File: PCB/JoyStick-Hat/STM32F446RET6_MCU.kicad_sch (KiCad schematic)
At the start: 42 parts, among them SW1 TL3301NF260QG, T1 BU2032SM-JJ-GTR, T2 20021121-00010C4LF, T3 0675031020, U1 STM32F446RET6, U11 AT24C16D-STUM-T, X1 ABM3B-8.000MHZ-B2-T, X2 ABS07-32.768KHZ-9-T

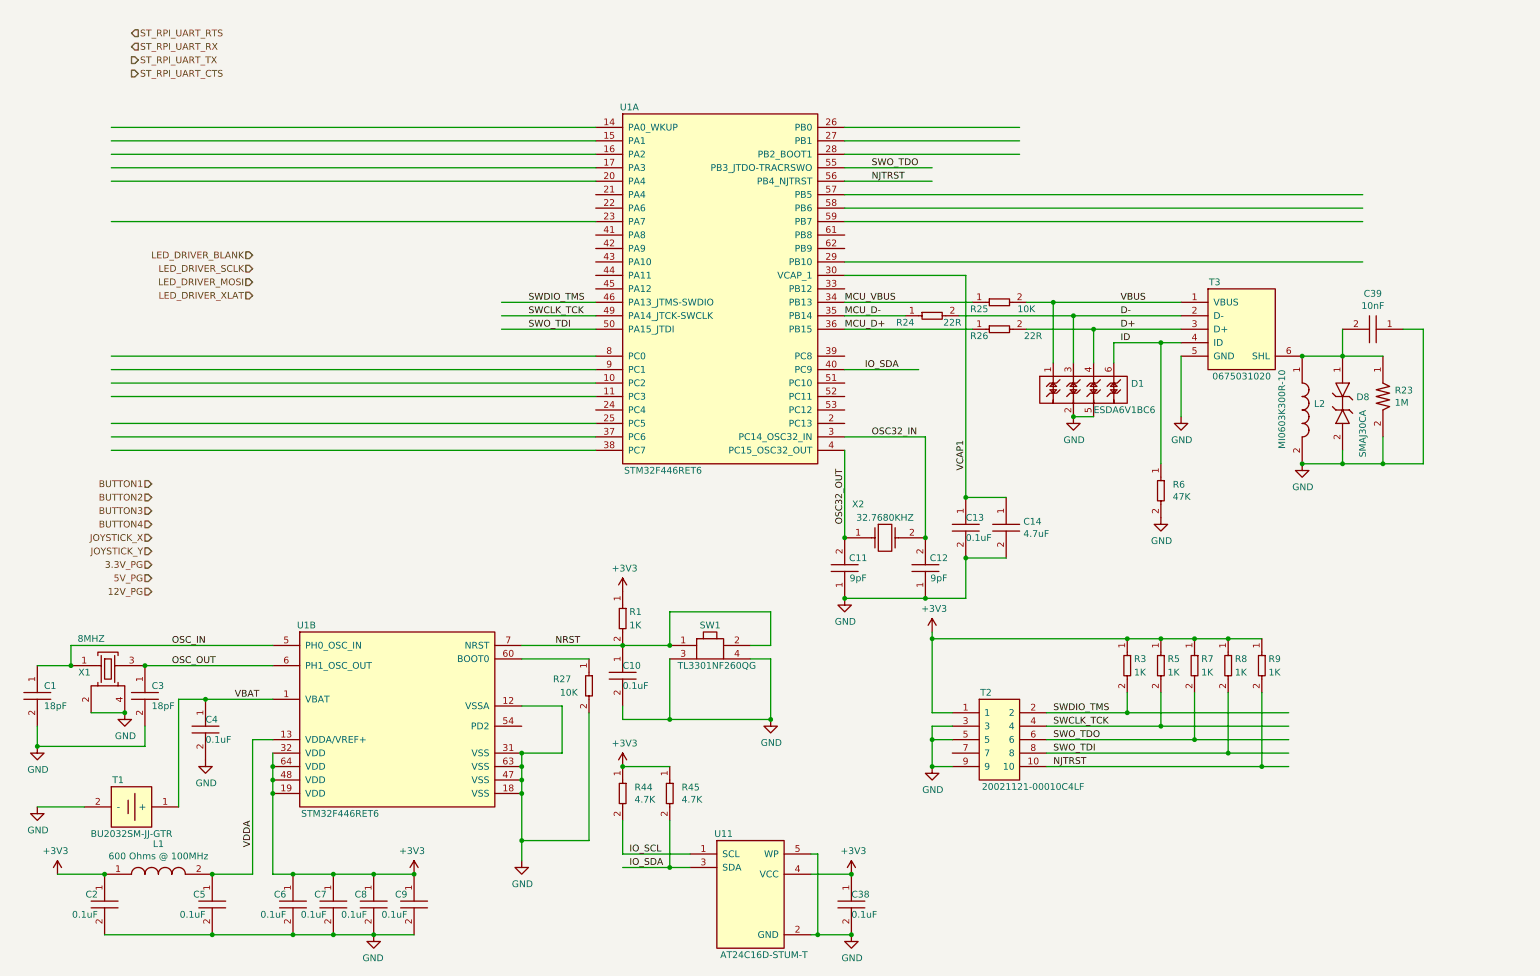
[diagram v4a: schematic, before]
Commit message: Schematic Progress
Made progress with schematic and corrected designator letters with connectors to match the built in paradigm of using J instead of T. T will not be used to referencing transformers instead of connectors.
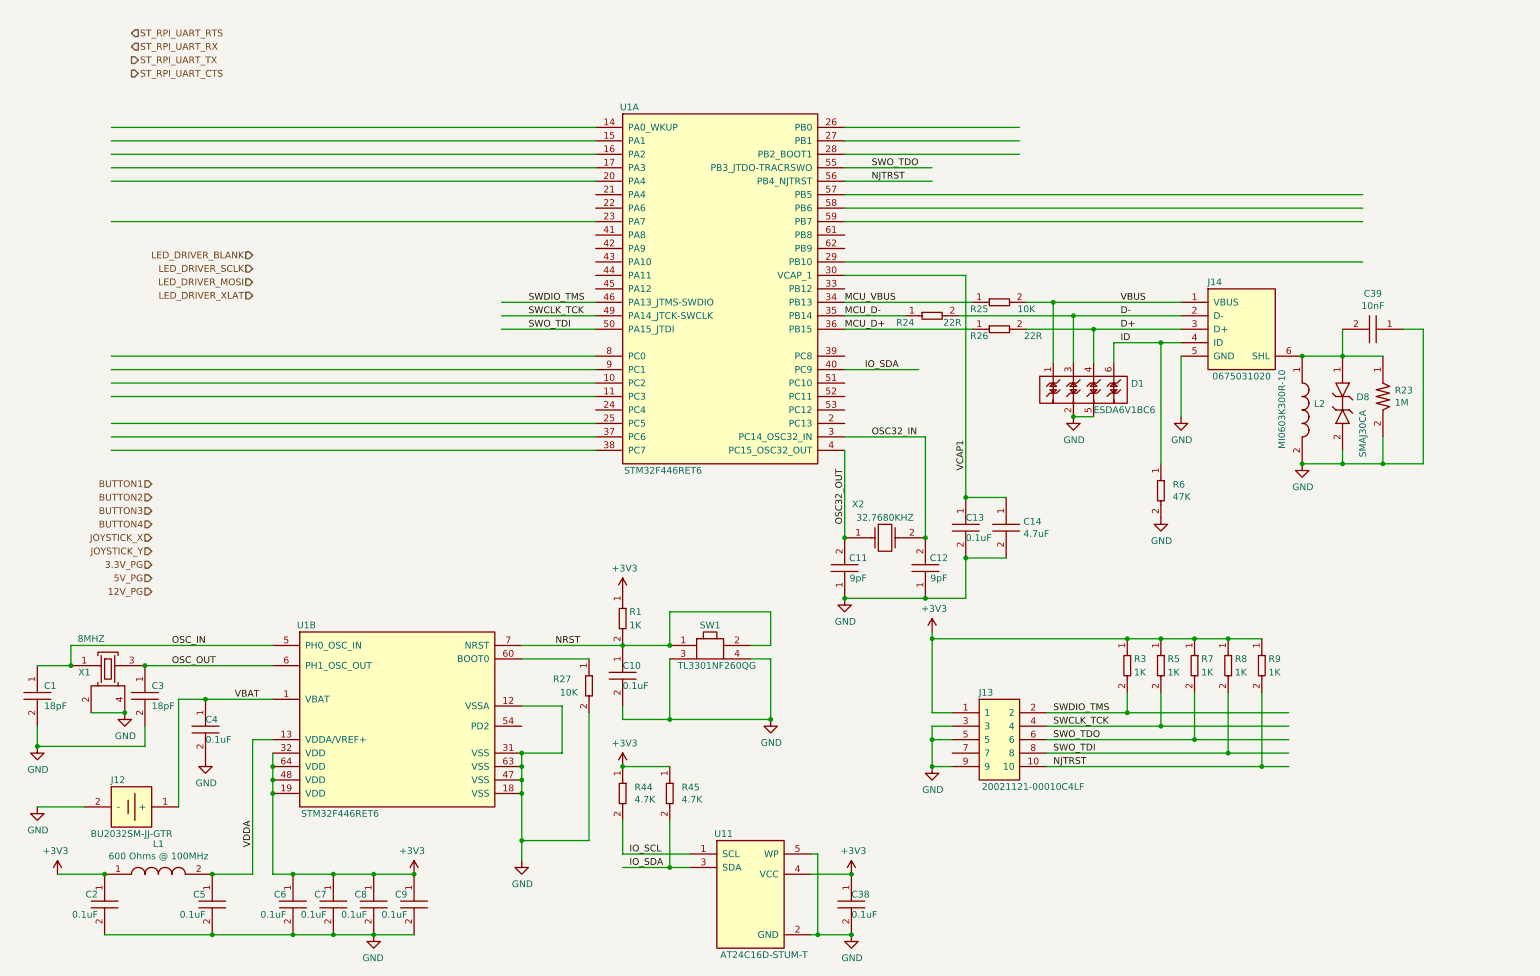
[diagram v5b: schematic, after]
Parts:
- removed T1: BU2032SM-JJ-GTR, AVR-KiCAD-Lib-Battery-Holders:BU2032SM-JJ-GTR, symbol AVR-KiCAD-Lib-Battery-Holders:BU2032SM-JJ-GTR
- added J12: BU2032SM-JJ-GTR, AVR-KiCAD-Lib-Connectors:BU2032SM-JJ-GTR, symbol AVR-KiCAD-Lib-Battery-Holders:BU2032SM-JJ-GTR
- renumbered T2 to J13, T3 to J14
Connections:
- net GND: now also J12.2 (-)
- net VBAT: now also J12.1 (+)
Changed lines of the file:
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@@
     )
   )
-  (symbol (lib_id "AVR-KiCAD-Lib-Battery-Holders:BU2032SM-JJ-GTR") (at 34.29 167.64 0) (unit 1)
-    (in_bom yes) (on_board yes) (dnp no)
-    (property "Reference" "T1" (at 31.75 162.56 0)
-      (effects (font (size 1.27 1.27)))
-    )
-    (property "Value" "BU2032SM-JJ-GTR" (at 34.29 172.72 0)
-      (effects (font (size 1.27 1.27)))
-    )
-    (property "Footprint" "AVR-KiCAD-Lib-Battery-Holders:BU2032SM-JJ-GTR" (at 31.75 158.75 0)
-      (effects (font (size 1.27 1.27)) hide)
-    )
-    (property "Datasheet" "http://www.memoryprotectiondevices.com/datasheets/BU2032SM-JJ-GTR-datasheet.pdf" (at 31.75 165.1 0)
-      (effects (font (size 1.27 1.27)) hide)
-    )
-    (property "Cost QTY: 1" "0.96000" (at 36.83 161.29 0)
-      (effects (font (size 1.27 1.27)) hide)
-    )
-    (property "Cost QTY: 1000" "*" (at 39.37 158.75 0)
-      (effects (font (size 1.27 1.27)) hide)
-    )
-    (property "Cost QTY: 2500" "*" (at 41.91 156.21 0)
-      (effects (font (size 1.27 1.27)) hide)
-    )
-    (property "Cost QTY: 5000" "*" (at 44.45 153.67 0)
-      (effects (font (size 1.27 1.27)) hide)
-    )
-    (property "Cost QTY: 10000" "*" (at 46.99 151.13 0)
-      (effects (font (size 1.27 1.27)) hide)
-    )
-    (property "MFR" "MPD (Memory Protection Devices)" (at 49.53 148.59 0)
-      (effects (font (size 1.27 1.27)) hide)
-    )
-    (property "MFR#" "BU2032SM-JJ-GTR" (at 52.07 146.05 0)
-      (effects (font (size 1.27 1.27)) hide)
-    )
-    (property "Vendor" "Digikey" (at 54.61 143.51 0)
-      (effects (font (size 1.27 1.27)) hide)
-    )
-    (property "Vendor #" "BU2032SM-JJ-GCT-ND" (at 57.15 140.97 0)
-      (effects (font (size 1.27 1.27)) hide)
-    )
-    (property "Designer" "AVR" (at 59.69 138.43 0)
-      (effects (font (size 1.27 1.27)) hide)
-    )
-    (property "Height" "5.3mm" (at 62.23 135.89 0)
-      (effects (font (size 1.27 1.27)) hide)
-    )
-    (property "Date Created" "12/7/2019" (at 90.17 107.95 0)
-      (effects (font (size 1.27 1.27)) hide)
-    )
-    (property "Date Modified" "12/7/2019" (at 64.77 133.35 0)
-      (effects (font (size 1.27 1.27)) hide)
-    )
-    (property "Lead-Free ?" "Yes" (at 67.31 130.81 0)
-      (effects (font (size 1.27 1.27)) hide)
-    )
-    (property "RoHS Levels" "1" (at 69.85 128.27 0)
-      (effects (font (size 1.27 1.27)) hide)
-    )
-    (property "Mounting" "SMT" (at 72.39 125.73 0)
-      (effects (font (size 1.27 1.27)) hide)
-    )
-    (property "Pin Count #" "2" (at 74.93 123.19 0)
-      (effects (font (size 1.27 1.27)) hide)
-    )
-    (property "Status" "Active" (at 77.47 120.65 0)
-      (effects (font (size 1.27 1.27)) hide)
-    )
-    (property "Tolerance" "*" (at 80.01 118.11 0)
-      (effects (font (size 1.27 1.27)) hide)
-    )
-    (property "Type" "Battery Clip" (at 82.55 115.57 0)
-      (effects (font (size 1.27 1.27)) hide)
-    )
-    (property "Voltage" "3.3V" (at 85.09 113.03 0)
-      (effects (font (size 1.27 1.27)) hide)
-    )
-    (property "Package" "Proprietary" (at 87.63 109.22 0)
-      (effects (font (size 1.27 1.27)) hide)
-    )
-    (property "Description" "Battery Holder (Open) Coin, 20.0mm 1 Cell SMD (SMT) Tab" (at 97.79 99.06 0)
-      (effects (font (size 1.27 1.27)) hide)
-    )
-    (property "_Value_" "Battery Clip" (at 92.71 104.14 0)
-      (effects (font (size 1.27 1.27)) hide)
-    )
-    (property "Management_ID" "*" (at 95.25 101.6 0)
-      (effects (font (size 1.27 1.27)) hide)
-    )
-    (pin "1")
-    (pin "2")
-    (instances
-      (project "JoyStick-Hat"
-        (path "/cf0c81b5-5bdf-47c3-83c0-f6980f515e65/edccb318-6986-4250-98d3-482c4b5ba7f8"
-          (reference "T1") (unit 1)
-        )
-      )
-      (project "agricoltura-vine"
-        (path "/d9101753-24ed-41f7-9f75-798d6e08c38a/00000000-0000-0000-0000-00005ee8264d"
-          (reference "T1") (unit 1)
-        )
-      )
-    )
-  )
   (symbol (lib_id "AVR-KiCAD-Lib-Oscillators-Clocks:ABM3B-8.000MHZ-B2-T") (at 27.94 138.43 0) (unit 1)
     (in_bom yes) (on_board yes) (dnp no)
@@
   (symbol (lib_id "AVR-KiCAD-Lib-Connectors:20021121-00010C4LF") (at 194.31 147.32 0) (unit 1)
     (in_bom yes) (on_board yes) (dnp no)
-    (property "Reference" "T2" (at 195.58 146.05 0)
+    (property "Reference" "J13" (at 195.58 146.05 0)
       (effects (font (size 1.27 1.27)))
     )
@@
       (project "JoyStick-Hat"
         (path "/cf0c81b5-5bdf-47c3-83c0-f6980f515e65/edccb318-6986-4250-98d3-482c4b5ba7f8"
-          (reference "T2") (unit 1)
+          (reference "J13") (unit 1)
         )
       )
@@
   (symbol (lib_id "AVR-KiCAD-Lib-Connectors:0675031020") (at 237.49 69.85 0) (unit 1)
     (in_bom yes) (on_board yes) (dnp no)
-    (property "Reference" "T3" (at 238.76 68.58 0)
+    (property "Reference" "J14" (at 238.76 68.58 0)
       (effects (font (size 1.27 1.27)))
     )
@@
       (project "JoyStick-Hat"
         (path "/cf0c81b5-5bdf-47c3-83c0-f6980f515e65/edccb318-6986-4250-98d3-482c4b5ba7f8"
-          (reference "T3") (unit 1)
+          (reference "J14") (unit 1)
         )
       )
@@
         )
       )
+    )
+  )
+  (symbol (lib_id "AVR-KiCAD-Lib-Battery-Holders:BU2032SM-JJ-GTR") (at 34.29 167.64 0) (unit 1)
+    (in_bom yes) (on_board yes) (dnp no)
+    (property "Reference" "J12" (at 31.75 162.56 0)
+      (effects (font (size 1.27 1.27)))
+    )
+    (property "Value" "BU2032SM-JJ-GTR" (at 34.29 172.72 0)
+      (effects (font (size 1.27 1.27)))
+    )
+    (property "Footprint" "AVR-KiCAD-Lib-Connectors:BU2032SM-JJ-GTR" (at 31.75 158.75 0)
+      (effects (font (size 1.27 1.27)) hide)
+    )
+    (property "Datasheet" "http://www.memoryprotectiondevices.com/datasheets/BU2032SM-JJ-GTR-datasheet.pdf" (at 31.75 165.1 0)
+      (effects (font (size 1.27 1.27)) hide)
+    )
+    (property "Cost QTY: 1" "0.96000" (at 36.83 161.29 0)
+      (effects (font (size 1.27 1.27)) hide)
+    )
+    (property "Cost QTY: 1000" "*" (at 39.37 158.75 0)
+      (effects (font (size 1.27 1.27)) hide)
+    )
+    (property "Cost QTY: 2500" "*" (at 41.91 156.21 0)
+      (effects (font (size 1.27 1.27)) hide)
+    )
+    (property "Cost QTY: 5000" "*" (at 44.45 153.67 0)
+      (effects (font (size 1.27 1.27)) hide)
+    )
+    (property "Cost QTY: 10000" "*" (at 46.99 151.13 0)
+      (effects (font (size 1.27 1.27)) hide)
+    )
+    (property "MFR" "MPD (Memory Protection Devices)" (at 49.53 148.59 0)
+      (effects (font (size 1.27 1.27)) hide)
+    )
+    (property "MFR#" "BU2032SM-JJ-GTR" (at 52.07 146.05 0)
+      (effects (font (size 1.27 1.27)) hide)
+    )
+    (property "Vendor" "Digikey" (at 54.61 143.51 0)
+      (effects (font (size 1.27 1.27)) hide)
+    )
+    (property "Vendor #" "BU2032SM-JJ-GCT-ND" (at 57.15 140.97 0)
+      (effects (font (size 1.27 1.27)) hide)
+    )
+    (property "Designer" "AVR" (at 59.69 138.43 0)
+      (effects (font (size 1.27 1.27)) hide)
+    )
+    (property "Height" "5.3mm" (at 62.23 135.89 0)
+      (effects (font (size 1.27 1.27)) hide)
+    )
+    (property "Date Created" "12/7/2019" (at 90.17 107.95 0)
+      (effects (font (size 1.27 1.27)) hide)
+    )
+    (property "Date Modified" "12/7/2019" (at 64.77 133.35 0)
+      (effects (font (size 1.27 1.27)) hide)
+    )
+    (property "Lead-Free ?" "Yes" (at 67.31 130.81 0)
+      (effects (font (size 1.27 1.27)) hide)
+    )
+    (property "RoHS Levels" "1" (at 69.85 128.27 0)
+      (effects (font (size 1.27 1.27)) hide)
+    )
+    (property "Mounting" "SMT" (at 72.39 125.73 0)
+      (effects (font (size 1.27 1.27)) hide)
+    )
+    (property "Pin Count #" "2" (at 74.93 123.19 0)
+      (effects (font (size 1.27 1.27)) hide)
+    )
+    (property "Status" "Active" (at 77.47 120.65 0)
+      (effects (font (size 1.27 1.27)) hide)
+    )
+    (property "Tolerance" "*" (at 80.01 118.11 0)
+      (effects (font (size 1.27 1.27)) hide)
+    )
+    (property "Type" "Battery Clip" (at 82.55 115.57 0)
+      (effects (font (size 1.27 1.27)) hide)
+    )
+    (property "Voltage" "3.3V" (at 85.09 113.03 0)
+      (effects (font (size 1.27 1.27)) hide)
+    )
+    (property "Package" "Proprietary" (at 87.63 109.22 0)
+      (effects (font (size 1.27 1.27)) hide)
+    )
+    (property "Description" "Battery Holder (Open) Coin, 20.0mm 1 Cell SMD (SMT) Tab" (at 97.79 99.06 0)
+      (effects (font (size 1.27 1.27)) hide)
+    )
+    (property "_Value_" "Battery Clip" (at 92.71 104.14 0)
+      (effects (font (size 1.27 1.27)) hide)
+    )
+    (property "Management_ID" "*" (at 95.25 101.6 0)
+      (effects (font (size 1.27 1.27)) hide)
+    )
+    (pin "1")
+    (pin "2")
+    (instances
+      (project "JoyStick-Hat"
+        (path "/cf0c81b5-5bdf-47c3-83c0-f6980f515e65/edccb318-6986-4250-98d3-482c4b5ba7f8"
+          (reference "J12") (unit 1)
+        )
+      )

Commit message: Schematic Complete
Schematic completed. Moved to 100 pin version of STM32 MCU for more connectivity and better muxing of internal peripherals with pins.
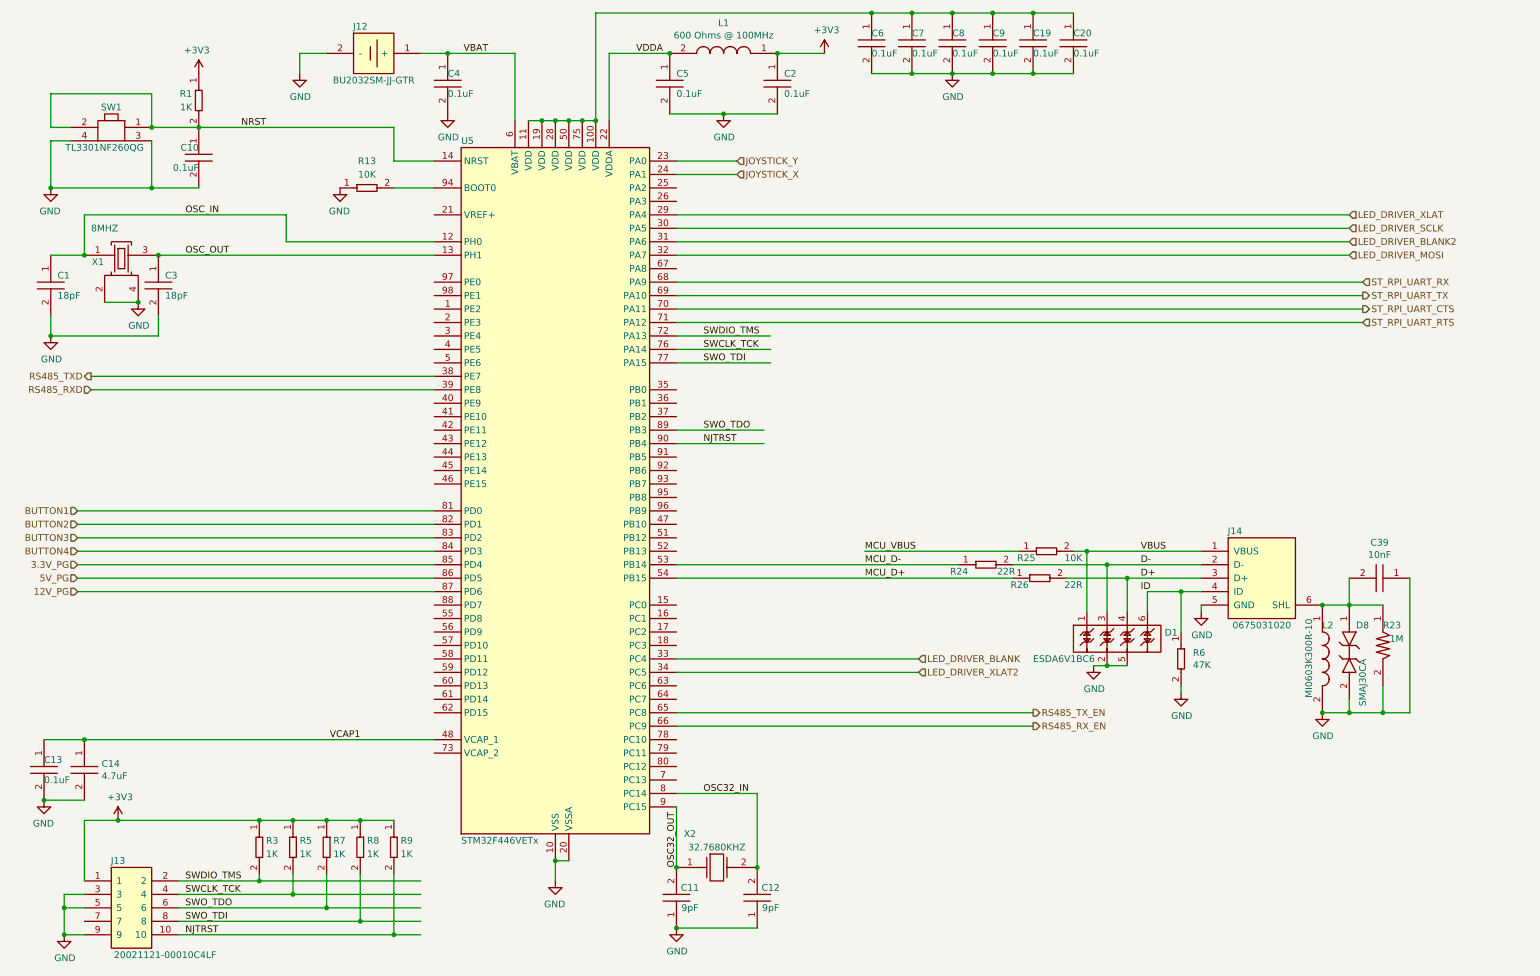
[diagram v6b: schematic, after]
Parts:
- removed C38: C0402C104K9PACTU, AVR-KiCAD-Lib-Resistors:R0402, symbol AVR-KiCAD-Lib-Capacitors:C0402C104K9PACTU
- removed R27: RC0402FR-0710KL, AVR-KiCAD-Lib-Resistors:R0402, symbol AVR-KiCAD-Lib-Resistors:RC0402FR-0710KL
- removed R44, R45: RC0402FR-074K7L, AVR-KiCAD-Lib-Resistors:R0402, symbol AVR-KiCAD-Lib-Resistors:RC0402FR-074K7L
- removed U1: STM32F446RET6, AVR-KiCAD-Lib-ICs:STM32F446RET6, symbol AVR-KiCAD-Lib-ICs:STM32F446RET6
- removed U11: AT24C16D-STUM-T, AVR-KiCAD-Lib-ICs:SOT-23-5, symbol AVR-KiCAD-Lib-ICs:AT24C16D-STUM-T
- added C19, C20: C0402C104K9PACTU, AVR-KiCAD-Lib-Resistors:R0402, symbol AVR-KiCAD-Lib-Capacitors:C0402C104K9PACTU
- added R13: RC0402FR-0710KL, AVR-KiCAD-Lib-Resistors:R0402, symbol AVR-KiCAD-Lib-Resistors:RC0402FR-0710KL
- added U5: STM32F446VETx, Package_QFP:LQFP-100_14x14mm_P0.5mm, symbol MCU_ST_STM32F4:STM32F446VETx
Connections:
- net +3V3: no longer C6.1, C7.1, C8.1, C9.1
- net 12V_PG: now also U5.87 (PD6)
- net 3.3V_PG: now also U5.85 (PD4)
- net 5V_PG: now also U5.86 (PD5)
- net BUTTON1: now also U5.81 (PD0)
- net BUTTON2: now also U5.82 (PD1)
- net BUTTON3: now also U5.83 (PD2)
- net BUTTON4: now also U5.84 (PD3)
- net GND: now also C19.2, C20.2, R13.1, U5.10 (VSS), U5.20 (VSSA), U5.27 (VSS), U5.49 (VSS), U5.74 (VSS), U5.99 (VSS)
- net ID: no longer D1.6, J14.4 (ID), R6.1
- net JOYSTICK_X: now also U5.24 (PA1)
- net JOYSTICK_Y: now also U5.23 (PA0)
- net LED_DRIVER_BLANK: now also U5.33 (PC4)
- net LED_DRIVER_MOSI: now also U5.32 (PA7)
- net LED_DRIVER_SCLK: now also U5.30 (PA5)
- net LED_DRIVER_XLAT: now also U5.29 (PA4)
- net MCU_D+: now also U5.54 (PB15)
- net MCU_D-: now also U5.53 (PB14)
- net NJTRST: now also U5.90 (PB4)
- net NRST: now also U5.14 (NRST)
- net OSC32_IN: now also U5.8 (PC14)
- net OSC32_OUT: now also U5.9 (PC15)
- net OSC_IN: now also U5.12 (PH0)
- net OSC_OUT: now also U5.13 (PH1)
- net ST_RPI_UART_CTS: now also U5.70 (PA11)
- net ST_RPI_UART_RTS: now also U5.71 (PA12)
- net ST_RPI_UART_RX: now also U5.68 (PA9)
- net ST_RPI_UART_TX: now also U5.69 (PA10)
- net SWCLK_TCK: now also U5.76 (PA14)
- net SWDIO_TMS: now also U5.72 (PA13)
- net SWO_TDI: now also U5.77 (PA15)
- net SWO_TDO: now also U5.89 (PB3)
- net VBAT: now also U5.6 (VBAT)
- net VCAP1: now also U5.48 (VCAP_1)
- net VDDA: now also U5.22 (VDDA)
- new net: D1.6, J14.4 (ID), R6.1
- new net: C19.1, C20.1, C6.1, C7.1, C8.1, C9.1, U5.100 (VDD), U5.11 (VDD), U5.19 (VDD), U5.28 (VDD), U5.50 (VDD), U5.75 (VDD)
- new net: R13.2, U5.94 (BOOT0)
- new net LED_DRIVER_BLANK2: U5.31 (PA6)
- new net LED_DRIVER_XLAT2: U5.34 (PC5)
- new net RS485_RXD: U5.39 (PE8)
- new net RS485_RX_EN: U5.66 (PC9)
- new net RS485_TXD: U5.38 (PE7)
- new net RS485_TX_EN: U5.65 (PC8)
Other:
- moved on the sheet: C1, C10, C11, C12, C13, C14, C2, C3, C39, C4, C5, D1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
